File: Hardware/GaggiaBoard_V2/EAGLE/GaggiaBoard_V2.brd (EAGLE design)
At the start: 102 x 92 mm, 106 parts, among them IC1 LD117AS33TR, J11 PIN262409-1, J12 PIN262409-1, J13 PIN262409-1, J14 PIN262409-1, J15 PIN262409-1, J16 PIN262409-1, J17 PIN262409-1, J18 PIN262409-1, J19 PIN262409-1, J2 Vertical Qwiic Connector, J20 PIN262409-1, J3 Vertical Qwiic Connector, J5 2PIN, J6 3PIN, J7 3PIN, J8 5PIN, J9 3PIN, K1 RELAY-SPDT-JZC-11F, K2 RELAY-SPDT-JZC-11F, K3 RELAY-SPDT-JZC-11F, Q1 600mA/40V, Q10 600mA/40V, Q2 600mA/40V, Q3 600mA/40V, Q4 600mA/40V, Q5 600mA/40V, Q6 600mA/40V, Q8 600mA/40V, Q9 600mA/40V, U1 BLACKPILL, U2 MAX31855K, U5 TXS0102

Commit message: J1 fix
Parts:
- J1: value (none) -> 4PIN; device SparkFun-Connectors:MOLEX-1X4 -> jst_exh:B4B-XH-K-S
- moved J1 3.75 mm to (99.0, 14.8)
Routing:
- net UART2_TX: track 48.2 -> 51.6 mm
- net UART2_RX: track 51.0 -> 47.7 mm
- net 5V: track 339.7 -> 336.5 mm
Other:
- board text added: "G TX RX 5V"
- board text removed: "5V RX TX G"
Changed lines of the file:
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@@
 <drawing>
 <settings>
-<setting alwaysvectorfont="no"/>
+<setting alwaysvectorfont="yes"/>
 <setting verticaltext="up"/>
 </settings>
@@
 </layers>
 <board>
-<fusionsync huburn="a.YnVzaW5lc3M6Z21haWwyMjIzNTY5" projecturn="a.YnVzaW5lc3M6Z21haWwyMjIzNTY5I0QyMDIyMDEwNDQ4MTQ5MTcwNg" f3durn="urn:adsk.wipprod:dm.lineage:6w6Byw4bTdmTaueqAgbUEw" pcbguid="" lastpulledtime="" lastsyncedchangeguid="" latestrevisionid="f5b72319-5f83-45ac-8c5c-21c1cc47dbd0" lastsyncedrevisionid="f5b72319-5f83-45ac-8c5c-21c1cc47dbd0" lastboardhashguid="f5f3250e-0ac0-ee41-2de5-6bbe57c72a9f" lastpushedtime="2022-08-14T00:36:34Z" linktopcb3d="true"/>
+<fusionsync huburn="a.YnVzaW5lc3M6Z21haWwyMjIzNTY5" projecturn="a.YnVzaW5lc3M6Z21haWwyMjIzNTY5I0QyMDIyMDEwNDQ4MTQ5MTcwNg" f3durn="urn:adsk.wipprod:dm.lineage:6w6Byw4bTdmTaueqAgbUEw" pcbguid="" lastpulledtime="" lastsyncedchangeguid="" latestrevisionid="3e8d3f7b-ea92-42a8-beec-9cc7b7c087b2" lastsyncedrevisionid="3e8d3f7b-ea92-42a8-beec-9cc7b7c087b2" lastboardhashguid="0d77b894-c7df-d1be-19fa-e803249ef199" lastpushedtime="2022-09-28T19:38:03Z" linktopcb3d="true"/>
 <plain>
 <wire x1="3.5" y1="0" x2="98.5" y2="0" width="0" layer="20"/>
@@
 NRST
 BOOT1</text>
-<text x="95.789" y="10.699" size="0.8128" layer="21" rot="R90">5V   RX   TX   G</text>
+<text x="95.408" y="10.826" size="0.8128" layer="21" rot="R90">G   TX   RX   5V</text>
 <text x="88.55" y="3.714" size="1.27" layer="21" rot="SR270">5V
 G
@@
 <attribute name="VALUE" x="47.54" y="61.3208" size="1.27" layer="27" rot="R180" display="off"/>
 </element>
-<element name="J1" library="SparkFun-Connectors" package="MOLEX-1X4" override_package3d_urn="urn:adsk.eagle:package:36462044/3" override_package_urn="urn:adsk.eagle:footprint:36462045/1" value="" x="99" y="11" smashed="yes" rot="R90">
-<attribute name="LCSC" value="C144395" x="226" y="127.84" size="1.778" layer="27" rot="R90" display="off"/>
-<attribute name="NAME" x="102.429" y="19.128" size="0.6096" layer="25" font="vector" ratio="20" rot="R90"/>
-<attribute name="PROD_ID" value="CONN-08186" x="226" y="127.84" size="1.778" layer="27" rot="R90" display="off"/>
-<attribute name="SF_ID" value="PRT-08231" x="226" y="127.84" size="1.778" layer="27" rot="R90" display="off"/>
-<attribute name="VALUE" x="102.429" y="13.286" size="0.6096" layer="27" font="vector" ratio="20" rot="R90"/>
-</element>
 <element name="J11" library="con-faston" library_urn="urn:adsk.eagle:library:144" package="62409-1" package3d_urn="urn:adsk.eagle:package:6760/1" override_package3d_urn="urn:adsk.eagle:package:36461337/2" override_package_urn="urn:adsk.eagle:footprint:6751/1" value="PIN262409-1" x="9" y="38" smashed="yes">
 <attribute name="LCSC" value="C86495" x="78.85" y="-72.49" size="1.778" layer="27" display="off"/>
@@
 </element>
 <element name="PSU1" library="discrete" package="IRM-10" override_package3d_urn="urn:adsk.eagle:package:36415007/2" override_package_urn="urn:adsk.eagle:footprint:36415008/1" override_locally_modified="yes" value="IRM-10-5" x="31" y="79" smashed="yes">
+<attribute name="LCSC" value="C2857903" x="31" y="79" size="1.778" layer="27" display="off"/>
 <attribute name="NAME" x="55.689" y="85.858" size="1.27" layer="25" rot="R90"/>
 <attribute name="SPICEPREFIX" value="E" x="31" y="79" size="1.778" layer="27" display="off"/>
@@
 <attribute name="VALUE" x="74.095" y="21.635" size="1.27" layer="27" rot="R270"/>
 </element>
+<element name="J1" library="jst_exh" package="B4B-XH-K-S" override_package3d_urn="urn:adsk.eagle:package:37572770/2" override_package_urn="urn:adsk.eagle:footprint:37572771/1" value="4PIN" x="99" y="14.75" smashed="yes" rot="R90">
+<attribute name="LCSC" value="C144395" x="99" y="14.75" size="1.778" layer="27" rot="R90" display="off"/>
+<attribute name="NAME" x="0.8" y="-8.85" size="1.27" layer="25"/>
+</element>
 </elements>
 <signals>
 <signal name="GND">
-<contactref element="J1" pad="4"/>
 <contactref element="J2" pad="1"/>
 <contactref element="J3" pad="1"/>
@@
 <wire x1="73" y1="6" x2="79" y2="6" width="0.254" layer="1"/>
 <wire x1="86" y1="6" x2="80" y2="6" width="0.254" layer="1"/>
-<via x="93" y="21" extent="1-16" drill="0.35"/>
+<via x="93" y="23" extent="1-16" drill="0.35"/>
 <via x="95" y="30" extent="1-16" drill="0.35"/>
 <wire x1="88" y1="85" x2="86.5099" y2="83.5099" width="0.254" layer="16"/>
 <wire x1="86.5099" y1="83.5099" x2="86.5099" y2="76.4901" width="0.254" layer="16"/>
+<contactref element="J1" pad="4"/>
 </signal>
 <signal name="5V">
-<contactref element="J1" pad="1"/>
 <contactref element="U1" pad="P1$18"/>
 <contactref element="U1" pad="P2$1"/>
@@
 <wire x1="99" y1="61" x2="96" y2="64" width="0.4064" layer="16"/>
 <wire x1="96" y1="64" x2="88" y2="64" width="0.4064" layer="16"/>
-<wire x1="99" y1="11" x2="95.9775" y2="14.0225" width="0.8128" layer="1"/>
-<wire x1="95.9775" y1="14.0225" x2="95.9775" y2="33.4975" width="0.8128" layer="1"/>
+<wire x1="95.9775" y1="14.0225" x2="95.9775" y2="20.193" width="0.8128" layer="1"/>
+<wire x1="95.9775" y1="20.193" x2="95.9775" y2="33.4975" width="0.8128" layer="1"/>
 <wire x1="87.75" y1="19.45" x2="87.75" y2="20.008" width="0.254" layer="1"/>
 <wire x1="87.75" y1="20.008" x2="87.534" y2="20.224" width="0.254" layer="1"/>
@@
 <wire x1="87.661" y1="12.985" x2="88" y2="13.324" width="0.254" layer="1"/>
 <wire x1="93" y1="6" x2="93" y2="7.9" width="0.6096" layer="1"/>
-<wire x1="93" y1="7.9" x2="92.233" y2="8.667" width="0.6096" layer="1"/>
-<wire x1="92.233" y1="8.667" x2="92.233" y2="11.207" width="0.6096" layer="1"/>
-<wire x1="92.876" y1="11.85" x2="94" y2="11.85" width="0.6096" layer="1"/>
-<wire x1="92.233" y1="11.207" x2="92.876" y2="11.85" width="0.6096" layer="1"/>
+<wire x1="92.233" y1="8.667" x2="93" y2="7.9" width="0.6096" layer="1"/>
 <contactref element="C8" pad="1"/>
 <wire x1="98.86" y1="36.38" x2="97.15" y2="34.67" width="0.8128" layer="1"/>
 <wire x1="97.15" y1="34.67" x2="97.15" y2="31.5" width="0.8128" layer="1"/>
-<wire x1="94" y1="11.85" x2="92.606" y2="11.85" width="0.254" layer="1"/>
-<wire x1="92.606" y1="11.85" x2="89.312" y2="15.144" width="0.508" layer="1"/>
-<wire x1="94" y1="11.85" x2="98.15" y2="11.85" width="0.6096" layer="1"/>
-<wire x1="98.15" y1="11.85" x2="99" y2="11" width="0.6096" layer="1"/>
+<contactref element="J1" pad="1"/>
+<wire x1="99" y1="18.5" x2="97.307" y2="20.193" width="0.8128" layer="1"/>
+<wire x1="97.307" y1="20.193" x2="95.9775" y2="20.193" width="0.8128" layer="1"/>
+<wire x1="94" y1="11.85" x2="94" y2="12.045" width="0.8128" layer="1"/>
+<wire x1="94" y1="12.045" x2="95.9775" y2="14.0225" width="0.8128" layer="1"/>
+<wire x1="94" y1="11.85" x2="93.365" y2="11.85" width="0.6096" layer="1"/>
+<wire x1="93.365" y1="11.85" x2="92.233" y2="10.718" width="0.6096" layer="1"/>
+<wire x1="92.233" y1="10.718" x2="92.233" y2="8.667" width="0.6096" layer="1"/>
+<wire x1="94" y1="11.85" x2="90.706" y2="15.144" width="0.6096" layer="1"/>
+<wire x1="90.706" y1="15.144" x2="89.312" y2="15.144" width="0.508" layer="1"/>
 </signal>
 <signal name="3V3">
@@
 <wire x1="79.533" y1="13.85" x2="81" y2="13.85" width="0.8128" layer="1"/>
 <wire x1="81" y1="13.85" x2="83" y2="13.85" width="0.8128" layer="1"/>
-<wire x1="92.68913125" y1="28" x2="87.239565625" y2="22.550434375" width="0.8128" layer="1"/>
-<wire x1="87.239565625" y1="22.550434375" x2="83" y2="18.31086875" width="0.8128" layer="1"/>
-<wire x1="92.68913125" y1="28" x2="94" y2="28" width="0.8128" layer="1"/>
-<wire x1="83" y1="13.85" x2="83" y2="18.31086875" width="0.8128" layer="1"/>
+<wire x1="93.07013125" y1="28" x2="87.430065625" y2="22.359934375" width="0.8128" layer="1"/>
+<wire x1="87.430065625" y1="22.359934375" x2="83" y2="17.92986875" width="0.8128" layer="1"/>
+<wire x1="93.07013125" y1="28" x2="94" y2="28" width="0.8128" layer="1"/>
+<wire x1="83" y1="13.85" x2="83" y2="17.92986875" width="0.8128" layer="1"/>
 <wire x1="88.25" y1="19.45" x2="88.25" y2="21.54" width="0.254" layer="1"/>
-<wire x1="88.25" y1="21.54" x2="87.239565625" y2="22.550434375" width="0.254" layer="1"/>
+<wire x1="88.25" y1="21.54" x2="87.430065625" y2="22.359934375" width="0.254" layer="1"/>
 <wire x1="76.478" y1="8.425" x2="76.478" y2="9.295" width="0.6096" layer="1"/>
 <wire x1="76.478" y1="9.295" x2="77.247" y2="10.064" width="0.6096" layer="1"/>
@@
 <via x="92" y="33" extent="1-16" drill="0.35"/>
 <wire x1="92" y1="31.984" x2="87.016" y2="27" width="0.254" layer="1"/>
-<wire x1="87.016" y1="27" x2="86" y2="27" width="0.254" layer="1"/>
+<wire x1="87.016" y1="27" x2="87" y2="27" width="0.254" layer="1"/>
 <wire x1="92" y1="33" x2="92" y2="31.984" width="0.254" layer="1"/>
-<via x="86" y="27" extent="1-16" drill="0.35"/>
+<via x="87" y="27" extent="1-16" drill="0.35"/>
 <contactref element="J1" pad="2"/>
-<wire x1="99" y1="13.54" x2="86" y2="26.54" width="0.254" layer="16"/>
-<wire x1="86" y1="26.54" x2="86" y2="27" width="0.254" layer="16"/>
+<wire x1="98" y1="16" x2="87" y2="27" width="0.254" layer="16"/>
+<wire x1="98" y1="16" x2="99" y2="16" width="0.254" layer="16"/>
 </signal>
 <signal name="UART2_TX">
@@
 <wire x1="89.857" y1="34.143" x2="69.601" y2="34.143" width="0.254" layer="16"/>
 <wire x1="91" y1="33" x2="91" y2="32" width="0.254" layer="1"/>
-<wire x1="87" y1="28" x2="91" y2="32" width="0.254" layer="1"/>
-<via x="87" y="28" extent="1-16" drill="0.35"/>
+<wire x1="86" y1="27" x2="91" y2="32" width="0.254" layer="1"/>
+<via x="86" y="27" extent="1-16" drill="0.35"/>
 <contactref element="J1" pad="3"/>
-<wire x1="99" y1="16.08" x2="98.92" y2="16.08" width="0.254" layer="16"/>
-<wire x1="98.92" y1="16.08" x2="87" y2="28" width="0.254" layer="16"/>
+<wire x1="99" y1="13.5" x2="90.826" y2="21.674" width="0.254" layer="16"/>
+<wire x1="86" y1="27" x2="90.826" y2="22.174" width="0.254" layer="16"/>
+<wire x1="90.826" y1="22.174" x2="90.826" y2="21.674" width="0.254" layer="16"/>
 </signal>
 <signal name="PB9">

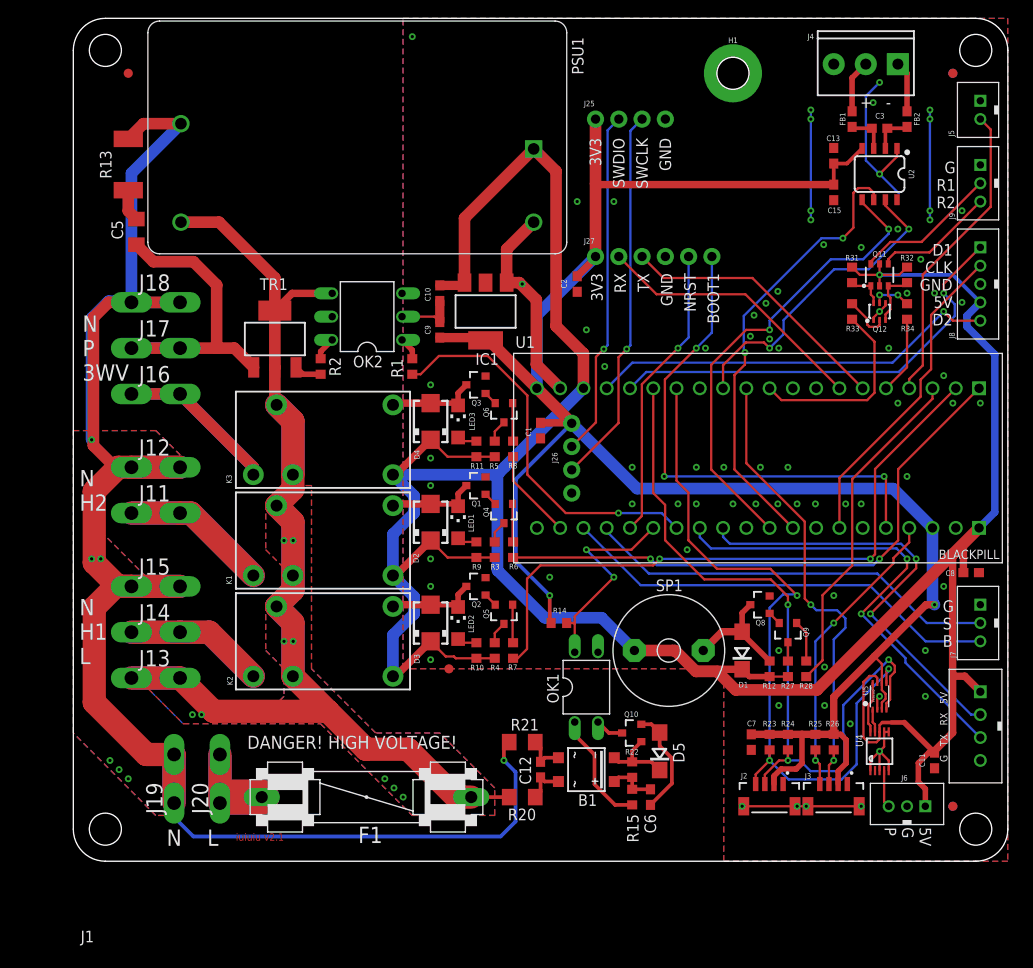
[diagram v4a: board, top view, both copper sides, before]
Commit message: 3-Way valve SSR
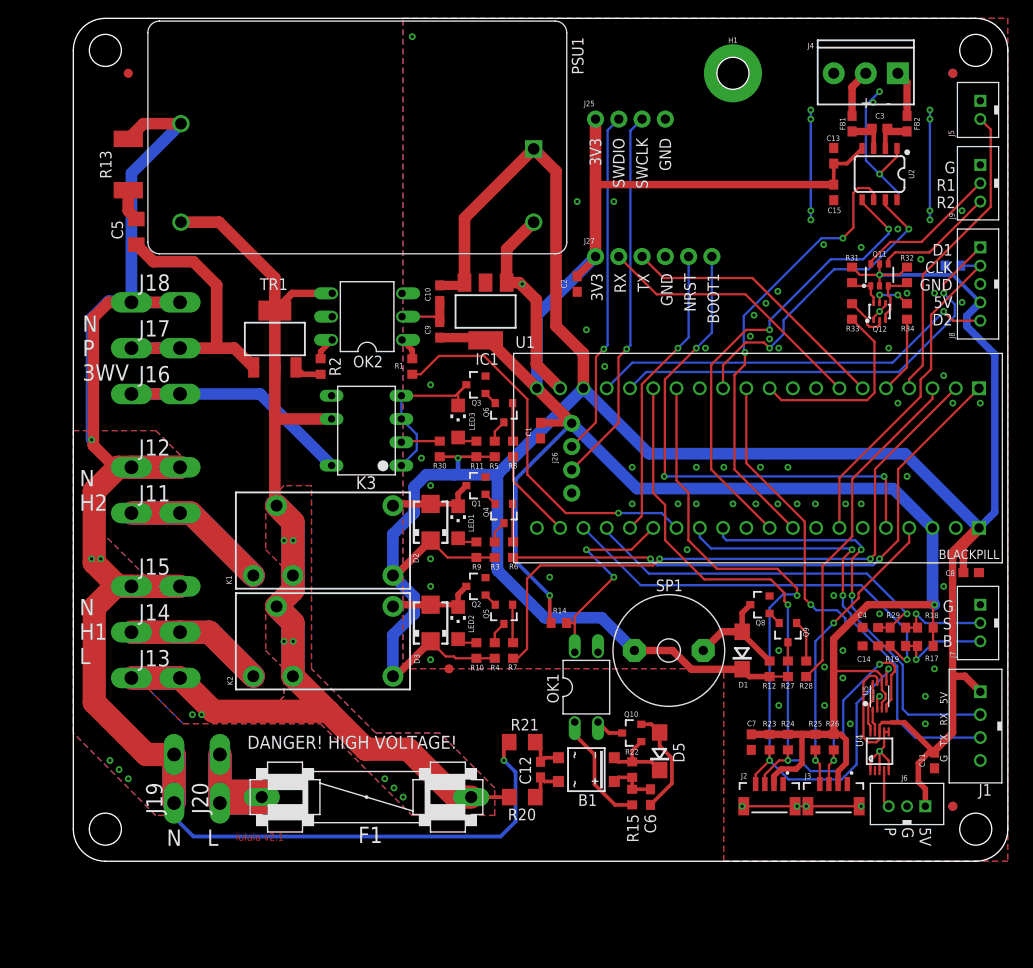
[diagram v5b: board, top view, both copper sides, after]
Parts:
- removed D4: S1M, diode:SMA
- added C14, C4: 0.01uF, rcl:C0603
- added R16: DNP, rcl:R0603
- added R17, R18, R19, R29: 10K, rcl:R0603
- added R30: 220, rcl:R0603
- K3: value RELAY-SPDT-JZC-11F -> AQH213; device SparkFun-Electromechanical:RELAY-JZC -> relay:DIL07
- moved K3 6.08 mm to (32.0, 47.0)
- moved J4 1.00 mm to (90.0, 86.0)
- moved FB1 0.50 mm to (85.0, 80.5)
- moved FB2 0.50 mm to (91.0, 80.5)
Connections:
- new net N$23: J7.2, R18.1, R29.1
- new net N$25: K3.2, R30.2
- new net N$6: J7.3, R17.1, R19.1
- net 3V3: now also R17.2, R18.2
- net 3WAY: now also K3.8; no longer K3.3
- net 5V: now also R16.1, R30.1; no longer D4.C, K3.5
- net AC_P: now also K3.6; no longer K3.2, K3.4
- net GND: now also C14.2, C4.2
- net N$12: now also K3.3, K3.4; no longer D4.A
- net PB0: now also R16.2
- net PC14: now also C14.1, R19.2; no longer J7.3
- net PC15: now also C4.1, R29.2; no longer J7.2
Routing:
- net 3V3: track 216.5 -> 227.8 mm
- net N$6: track 0.00 -> 10.7 mm, vias 0 -> 1
- net N$23: track 0.00 -> 10.3 mm, vias 0 -> 1
- net N$12: track 9.92 -> 19.2 mm
- net PC15: track 45.3 -> 40.7 mm, vias 0 -> 1
- net 3WAY: track 34.8 -> 30.4 mm
- net N$25: track 0.00 -> 4.24 mm
- net AC_P: track 153.6 -> 150.0 mm
- net 5V: track 336.5 -> 339.2 mm, vias 1 -> 2
- net PB0: track 35.0 -> 37.1 mm
- net UART2_TX: track 51.6 -> 49.5 mm
- net UART2_RX: track 47.7 -> 45.7 mm
- net PC14: track 48.4 -> 46.9 mm, vias 0 -> 1
- net GND: track 98.0 -> 97.0 mm, vias 77 -> 81
- net N$4: track 5.77 -> 5.27 mm
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
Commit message: snubbers
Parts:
- added C16: 10nF, rcl:C1206
- added R35: 220, rcl:R2512
- moved C5 27.7 mm to (19.5, 44.0), turned to 90 degrees
- moved R13 27.5 mm to (21.0, 53.0), turned to 180 degrees
- moved TR1 4.00 mm to (22.0, 61.0)
- turned R2 to 90 degrees
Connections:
- removed net N$32: C5.1, R13.2
- new net N$27: C5.2, R13.1
- new net N$31: C16.2, R35.1
- net 3WAY: now also R35.2
- net AC_N: no longer R13.1
- net AC_P: now also C16.1, C5.1
- net PUMP_P: now also R13.2; no longer C5.2
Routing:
- net PUMP_P: track 37.0 -> 23.0 mm
- net AC_P: track 150.0 -> 159.7 mm
- net N$27: track 0.00 -> 9.53 mm
- net 3WAY: track 30.4 -> 37.8 mm
- net AC_N: track 207.3 -> 200.9 mm
- net N$31: track 0.00 -> 4.14 mm
- net N$32: track 3.52 -> 0.00 mm
- net N$8: track 2.57 -> 4.60 mm
- net N$9: track 3.00 -> 4.47 mm

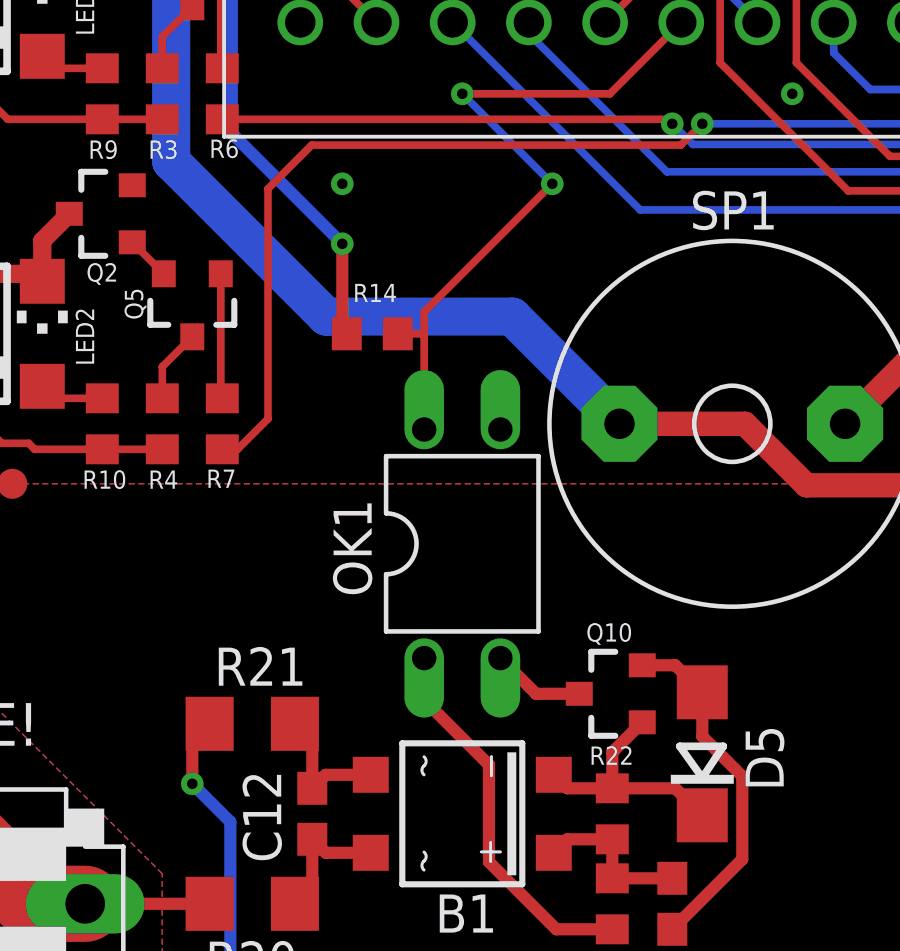
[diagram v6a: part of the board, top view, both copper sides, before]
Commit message: OK1 part change
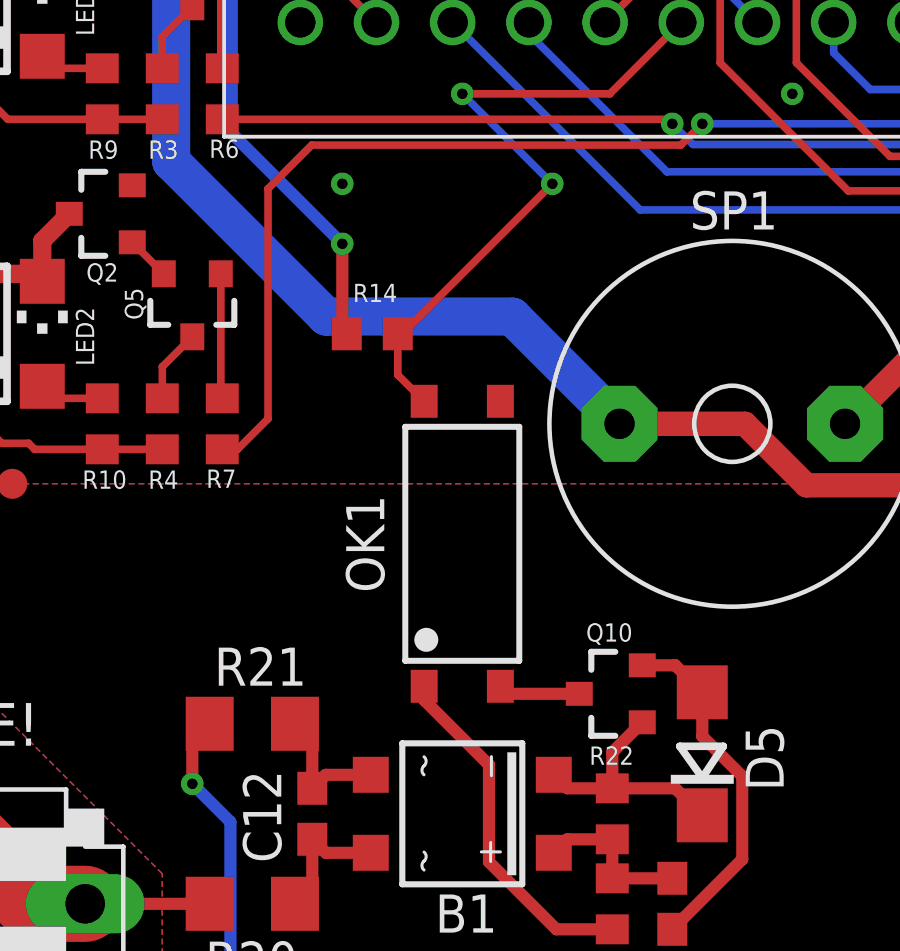
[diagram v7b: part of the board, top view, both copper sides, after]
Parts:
- OK1: value LTV816 -> 140106146000; device optocoupler:DIL04 -> Wurth_Optocoupler_WL-OCPT:WL-OCPT_LSOP4
- turned OK1 to 90 degrees
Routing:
- net PA0: track 23.4 -> 22.4 mm
- net N$44: track 12.7 -> 11.8 mm
